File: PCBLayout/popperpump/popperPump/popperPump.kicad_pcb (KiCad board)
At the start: 2 copper layers, 110 x 73 mm, 14 parts, among them M5StackHeader1 M5StackGPIO

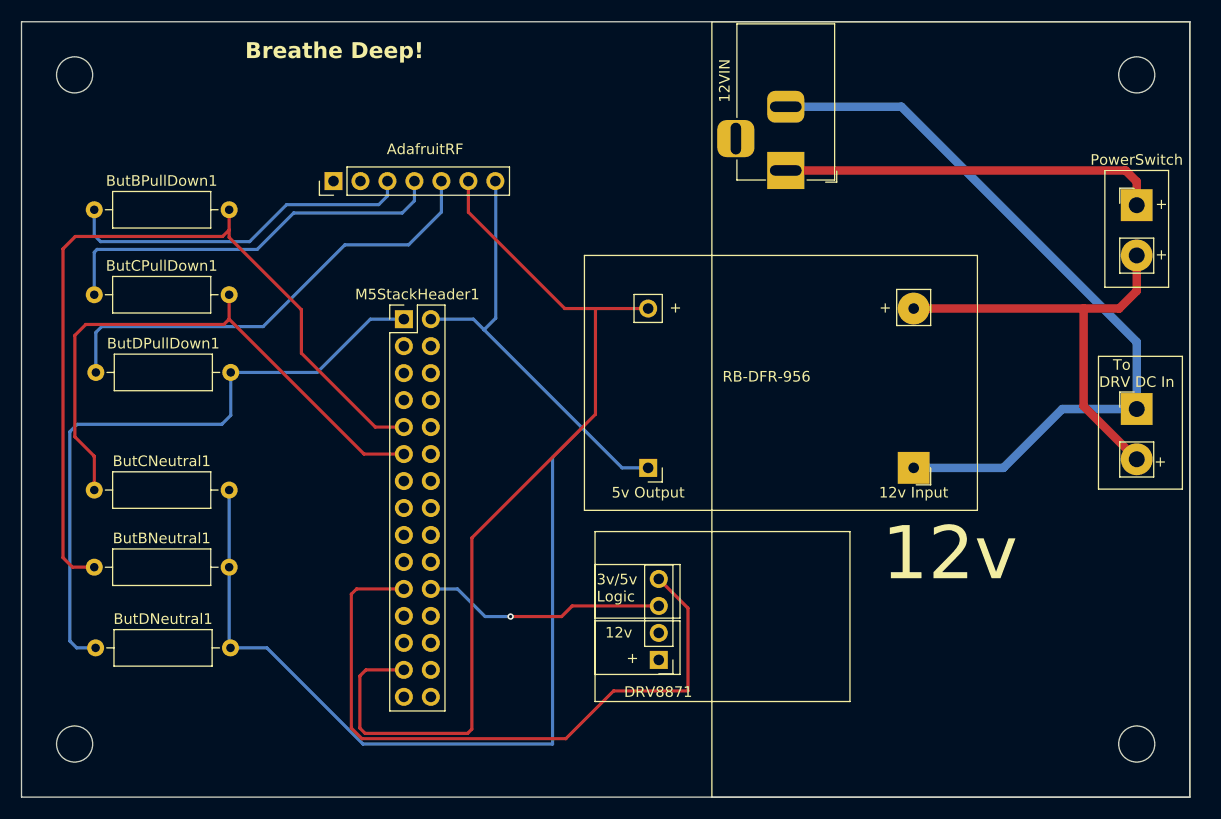
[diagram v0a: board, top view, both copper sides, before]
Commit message: 2 Fixes
 - Fix the PCB layout, one of the pins was placed wrong :facepalm:

- Remove the timing limits (coming later)

- Update GPIO pin layout for buttons, because I'm dumb
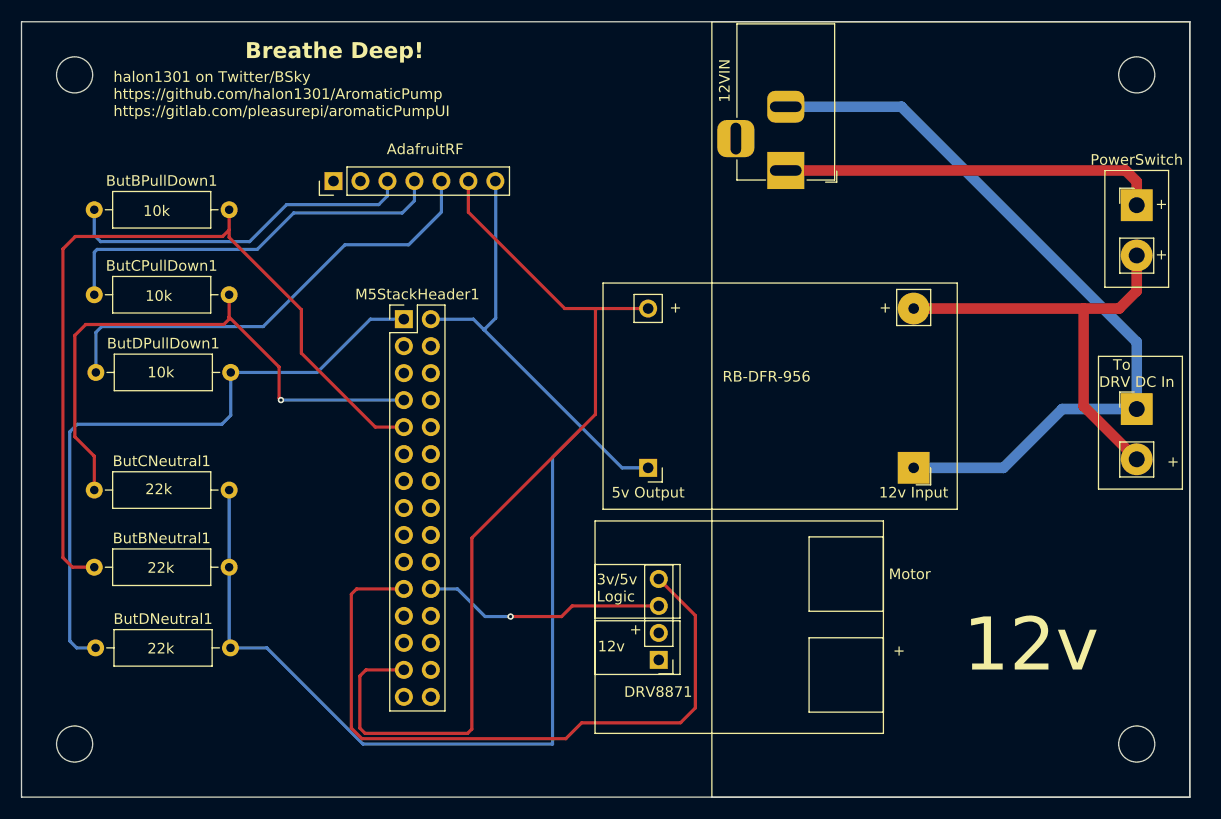
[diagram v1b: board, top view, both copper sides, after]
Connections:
- ButCNeutral1 pad 1: Net-(M5StackHeader1-Pin_11) -> Net-(M5StackHeader1-Pin_7)
- ButCPullDown1 pad 2: Net-(M5StackHeader1-Pin_11) -> Net-(M5StackHeader1-Pin_7)
- M5StackHeader1 pad 11: Net-(M5StackHeader1-Pin_11) -> unconnected-(M5StackHeader1-Pin_11-Pad11)
- M5StackHeader1 pad 7: unconnected-(M5StackHeader1-Pin_7-Pad7) -> Net-(M5StackHeader1-Pin_7)
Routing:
- net Net-(M5StackHeader1-Pin_11): track 54.5 -> 0.00 mm
- net Net-(M5StackHeader1-Pin_7): track 0.00 -> 54.2 mm, vias 0 -> 1
- net Net-(DRV8871-Pin_4): track 63.4 -> 65.3 mm
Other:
- board text added: "10k"
- board text added: "22k"
- board text added: "Motor"
- board text added: "halon1301 on Twitter/BSky https://github.com/halon1301/AromaticPump https://gitlab.com/pleasurepi/aromaticPumpUI"
